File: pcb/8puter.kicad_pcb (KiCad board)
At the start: 2 copper layers, 13 parts

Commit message: Memory Module
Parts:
- removed C4: ~, Capacitor_THT:CP_Radial_D4.0mm_P1.50mm
- removed UMUX1: 74LS151, Package_DIP:DIP-18_W7.62mm_SMDSocket_SmallPads
- removed UPWR1 (x2): LT1761-1.5, Package_TO_SOT_SMD:TSOT-23-5
- added C1: C_Polarized_Small, Capacitor_THT:CP_Radial_D5.0mm_P2.00mm, F.Cu at (91.4, 106.7)
- added PWREG1: LT1761-1.5, Package_TO_SOT_SMD:TSOT-23-5, F.Cu at (94.0, 97.8)
- added PWREG2: LT1962-5, Package_SO:MSOP-8_3x3mm_P0.65mm, F.Cu at (94.0, 114.3)
- added UA1: ~, Package_SO:SO-14_3.9x8.65mm_P1.27mm, F.Cu at (135.9, 111.8)
- added UDEC1: 74HC237, Package_SO:SOP-16_4.4x10.4mm_P1.27mm, F.Cu at (144.8, 95.2)
- added UI1: ~, Package_SO:SO-16_3.9x9.9mm_P1.27mm, F.Cu at (144.8, 111.8)
- moved RAM3 72.5 mm to (175.3, 106.7), turned to 0 degrees
- moved C3 62.6 mm to (163.8, 58.4), turned to -90 degrees
- moved C3 57.5 mm to (154.9, 61.3), turned to -90 degrees
- moved RAM0 55.5 mm to (160.0, 106.7), turned to 0 degrees
- moved RAM1 53.9 mm to (160.0, 83.8), turned to 0 degrees
- moved RAM2 52.9 mm to (175.3, 83.8), turned to 0 degrees
- moved ROM1 47.4 mm to (102.9, 61.0)
- moved CPU1 23.9 mm to (132.1, 77.5), turned to 180 degrees
- moved UCLK1 3.18 mm to (105.4, 115.6)
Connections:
- net /D3 renamed DATA3
- net /D4 renamed DATA4
- net /D5 renamed DATA5
- net /D6 renamed DATA6
- net /D7 renamed DATA7
- C3 pad 1: unconnected-(C3-Pad1) -> /Power/BOARD_IN (x2)
- C3 pad 2: unconnected-(C3-Pad2) -> GND (x2)
- CPU1 pad 10: /A5 -> ADDR5
- CPU1 pad 11: /A6 -> ADDR6
- CPU1 pad 12: /A7 -> ADDR7
- CPU1 pad 13: /A8 -> ADDR8
- CPU1 pad 14: /A9 -> ADDR9
- CPU1 pad 15: /A10 -> ADDR10
- CPU1 pad 16: /A11 -> ADDR11
- CPU1 pad 19: /A12 -> ADDR12
- CPU1 pad 20: /A13 -> ADDR13
- CPU1 pad 21: /A14 -> ADDR14
- CPU1 pad 22: /A15 -> ADDR15
- CPU1 pad 28: /D2 -> DATA2
- CPU1 pad 29: /D1 -> DATA1
- CPU1 pad 30: /D0 -> DATA0
- CPU1 pad 34: unconnected-(CPU1-Pad34) -> A/~{D}
- CPU1 pad 4: /A0 -> ADDR0
- CPU1 pad 43: unconnected-(CPU1-Pad43) -> ~{IRQ}
- CPU1 pad 5: /A1 -> ADDR1
- CPU1 pad 7: /A2 -> ADDR2
- CPU1 pad 8: /A3 -> ADDR3
- CPU1 pad 9: /A4 -> ADDR4
- RAM0 pad 1: unconnected-(RAM0-Pad1) -> DATA1
- RAM0 pad 10: /Memory Unit/A2 -> ADDR2
- RAM0 pad 11: /Memory Unit/A1 -> ADDR1
- RAM0 pad 12: /Memory Unit/A0 -> ADDR0
- RAM0 pad 13: /Memory Unit/D0 -> DATA0
- RAM0 pad 14: /Memory Unit/D1 -> DATA1
- RAM0 pad 15: /Memory Unit/D2 -> DATA2
- RAM0 pad 17: /Memory Unit/D3 -> DATA0
- RAM0 pad 18: /Memory Unit/D4 -> DATA0
- RAM0 pad 19: /Memory Unit/D5 -> DATA0
- RAM0 pad 2: unconnected-(RAM0-Pad2) -> DATA0
- RAM0 pad 20: /Memory Unit/D6 -> DATA0
- RAM0 pad 21: /Memory Unit/D7 -> DATA0
- RAM0 pad 22: unconnected-(RAM0-Pad22) -> /Memory Unit/~{RAM0_EN}
- RAM0 pad 23: /Memory Unit/A10 -> ADDR10
- RAM0 pad 24: READ -> /Memory Unit/~{RAM0_EN}
- RAM0 pad 25: /Memory Unit/A11 -> ADDR11
- RAM0 pad 26: /Memory Unit/A9 -> ADDR9
- RAM0 pad 27: /Memory Unit/A8 -> ADDR8
- RAM0 pad 28: /Memory Unit/A13 -> ADDR13
- RAM0 pad 29: unconnected-(RAM0-Pad29) -> /Memory Unit/CPU_W/~{R}
- RAM0 pad 3: /Memory Unit/A14 -> ADDR14
- RAM0 pad 30: unconnected-(RAM0-Pad30) -> DATA2
- RAM0 pad 31: /Memory Unit/A15 -> ADDR15
- RAM0 pad 4: /Memory Unit/A12 -> ADDR12
- RAM0 pad 5: /Memory Unit/A7 -> ADDR7
- RAM0 pad 6: /Memory Unit/A6 -> ADDR6
- RAM0 pad 7: /Memory Unit/A5 -> ADDR5
- RAM0 pad 8: /Memory Unit/A4 -> ADDR4
- RAM0 pad 9: /Memory Unit/A3 -> ADDR3
- RAM1 pad 1: unconnected-(RAM1-Pad1) -> DATA1
- RAM1 pad 10: /Memory Unit/A2 -> ADDR2
- RAM1 pad 11: /Memory Unit/A1 -> ADDR1
- RAM1 pad 12: /Memory Unit/A0 -> ADDR0
- RAM1 pad 13: /Memory Unit/D0 -> DATA0
- RAM1 pad 14: /Memory Unit/D1 -> DATA1
- RAM1 pad 15: /Memory Unit/D2 -> DATA2
- RAM1 pad 17: /Memory Unit/D3 -> DATA0
- RAM1 pad 18: /Memory Unit/D4 -> DATA0
- RAM1 pad 19: /Memory Unit/D5 -> DATA0
- RAM1 pad 2: unconnected-(RAM1-Pad2) -> DATA0
- RAM1 pad 20: /Memory Unit/D6 -> DATA0
- RAM1 pad 21: /Memory Unit/D7 -> DATA0
- RAM1 pad 22: unconnected-(RAM1-Pad22) -> /Memory Unit/~{RAM1_EN}
- RAM1 pad 23: /Memory Unit/A10 -> ADDR10
- RAM1 pad 24: READ -> /Memory Unit/~{RAM1_EN}
- RAM1 pad 25: /Memory Unit/A11 -> ADDR11
- RAM1 pad 26: /Memory Unit/A9 -> ADDR9
- RAM1 pad 27: /Memory Unit/A8 -> ADDR8
- RAM1 pad 28: /Memory Unit/A13 -> ADDR13
- RAM1 pad 29: unconnected-(RAM1-Pad29) -> /Memory Unit/CPU_W/~{R}
- RAM1 pad 3: /Memory Unit/A14 -> ADDR14
- RAM1 pad 30: unconnected-(RAM1-Pad30) -> DATA2
- RAM1 pad 31: /Memory Unit/A15 -> ADDR15
- RAM1 pad 4: /Memory Unit/A12 -> ADDR12
- RAM1 pad 5: /Memory Unit/A7 -> ADDR7
- RAM1 pad 6: /Memory Unit/A6 -> ADDR6
- RAM1 pad 7: /Memory Unit/A5 -> ADDR5
- RAM1 pad 8: /Memory Unit/A4 -> ADDR4
- RAM1 pad 9: /Memory Unit/A3 -> ADDR3
- RAM2 pad 1: unconnected-(RAM2-Pad1) -> DATA1
- RAM2 pad 10: /Memory Unit/A2 -> ADDR2
- RAM2 pad 11: /Memory Unit/A1 -> ADDR1
- RAM2 pad 12: /Memory Unit/A0 -> ADDR0
- RAM2 pad 13: /Memory Unit/D0 -> DATA0
- RAM2 pad 14: /Memory Unit/D1 -> DATA1
- RAM2 pad 15: /Memory Unit/D2 -> DATA2
- RAM2 pad 17: /Memory Unit/D3 -> DATA0
- RAM2 pad 18: /Memory Unit/D4 -> DATA0
- RAM2 pad 19: /Memory Unit/D5 -> DATA0
- RAM2 pad 2: unconnected-(RAM2-Pad2) -> DATA0
- RAM2 pad 20: /Memory Unit/D6 -> DATA0
- RAM2 pad 21: /Memory Unit/D7 -> DATA0
- RAM2 pad 22: unconnected-(RAM2-Pad22) -> /Memory Unit/~{RAM2_EN}
- RAM2 pad 23: /Memory Unit/A10 -> ADDR10
- RAM2 pad 24: READ -> /Memory Unit/~{RAM2_EN}
- RAM2 pad 25: /Memory Unit/A11 -> ADDR11
- RAM2 pad 26: /Memory Unit/A9 -> ADDR9
- RAM2 pad 27: /Memory Unit/A8 -> ADDR8
- RAM2 pad 28: /Memory Unit/A13 -> ADDR13
- RAM2 pad 29: unconnected-(RAM2-Pad29) -> /Memory Unit/CPU_W/~{R}
- RAM2 pad 3: /Memory Unit/A14 -> ADDR14
- RAM2 pad 30: unconnected-(RAM2-Pad30) -> DATA2
- RAM2 pad 31: /Memory Unit/A15 -> ADDR15
- RAM2 pad 4: /Memory Unit/A12 -> ADDR12
- RAM2 pad 5: /Memory Unit/A7 -> ADDR7
- RAM2 pad 6: /Memory Unit/A6 -> ADDR6
- RAM2 pad 7: /Memory Unit/A5 -> ADDR5
- RAM2 pad 8: /Memory Unit/A4 -> ADDR4
- RAM2 pad 9: /Memory Unit/A3 -> ADDR3
- RAM3 pad 1: unconnected-(RAM3-Pad1) -> DATA1
- RAM3 pad 10: /Memory Unit/A2 -> ADDR2
- RAM3 pad 11: /Memory Unit/A1 -> ADDR1
- RAM3 pad 12: /Memory Unit/A0 -> ADDR0
- RAM3 pad 13: /Memory Unit/D0 -> DATA0
- RAM3 pad 14: /Memory Unit/D1 -> DATA1
- RAM3 pad 15: /Memory Unit/D2 -> DATA2
- RAM3 pad 17: /Memory Unit/D3 -> DATA0
- RAM3 pad 18: /Memory Unit/D4 -> DATA0
- RAM3 pad 19: /Memory Unit/D5 -> DATA0
- RAM3 pad 2: unconnected-(RAM3-Pad2) -> DATA0
- RAM3 pad 20: /Memory Unit/D6 -> DATA0
- RAM3 pad 21: /Memory Unit/D7 -> DATA0
- RAM3 pad 22: unconnected-(RAM3-Pad22) -> /Memory Unit/~{RAM3_EN}
- RAM3 pad 23: /Memory Unit/A10 -> ADDR10
- RAM3 pad 24: READ -> /Memory Unit/~{RAM3_EN}
- RAM3 pad 25: /Memory Unit/A11 -> ADDR11
- RAM3 pad 26: /Memory Unit/A9 -> ADDR9
- RAM3 pad 27: /Memory Unit/A8 -> ADDR8
- RAM3 pad 28: /Memory Unit/A13 -> ADDR13
- RAM3 pad 29: unconnected-(RAM3-Pad29) -> /Memory Unit/CPU_W/~{R}
- RAM3 pad 3: /Memory Unit/A14 -> ADDR14
- RAM3 pad 30: unconnected-(RAM3-Pad30) -> DATA2
- RAM3 pad 31: /Memory Unit/A15 -> ADDR15
- RAM3 pad 4: /Memory Unit/A12 -> ADDR12
- RAM3 pad 5: /Memory Unit/A7 -> ADDR7
- RAM3 pad 6: /Memory Unit/A6 -> ADDR6
- RAM3 pad 7: /Memory Unit/A5 -> ADDR5
- RAM3 pad 8: /Memory Unit/A4 -> ADDR4
- RAM3 pad 9: /Memory Unit/A3 -> ADDR3
- ROM1 pad 10: /Memory Unit/A2 -> ADDR2
- ROM1 pad 11: /Memory Unit/A1 -> ADDR1
- ROM1 pad 12: /Memory Unit/A0 -> ADDR0
- ROM1 pad 13: /Memory Unit/D0 -> DATA0
- ROM1 pad 14: /Memory Unit/D1 -> DATA1
- ROM1 pad 15: /Memory Unit/D2 -> DATA2
- ROM1 pad 17: /Memory Unit/D3 -> DATA0
- ROM1 pad 18: /Memory Unit/D4 -> DATA0
- ROM1 pad 19: /Memory Unit/D5 -> DATA0
- ROM1 pad 2: unconnected-(ROM1-Pad2) -> /Memory Unit/CROM_EN
- ROM1 pad 20: /Memory Unit/D6 -> DATA0
- ROM1 pad 21: /Memory Unit/D7 -> DATA0
- ROM1 pad 22: unconnected-(ROM1-Pad22) -> /Memory Unit/ROM_EN
- ROM1 pad 23: /Memory Unit/A10 -> ADDR10
- ROM1 pad 24: READ -> R/~{W}
- ROM1 pad 25: /Memory Unit/A11 -> ADDR11
- ROM1 pad 26: /Memory Unit/A9 -> ADDR9
- ROM1 pad 27: /Memory Unit/A8 -> ADDR8
- ROM1 pad 28: /Memory Unit/A13 -> ADDR13
- ROM1 pad 29: /Memory Unit/A14 -> ADDR14
- ROM1 pad 3: /Memory Unit/A15 -> ADDR15
- ROM1 pad 31: READ -> unconnected-(ROM1-Pad31)
- ROM1 pad 4: /Memory Unit/A12 -> ADDR12
- ROM1 pad 5: /Memory Unit/A7 -> ADDR7
- ROM1 pad 6: /Memory Unit/A6 -> ADDR6
- ROM1 pad 7: /Memory Unit/A5 -> ADDR5
- ROM1 pad 8: /Memory Unit/A4 -> ADDR4
- ROM1 pad 9: /Memory Unit/A3 -> ADDR3
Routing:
- net ADDR4: track 0.00 -> 21.7 mm, vias 0 -> 2
- net ADDR5: track 0.00 -> 21.7 mm, vias 0 -> 2
- net ADDR6: track 0.00 -> 21.5 mm, vias 0 -> 2
- net unconnected-(CPU1-Pad41): track 19.5 -> 0.00 mm
- net unconnected-(CPU1-Pad42): track 18.7 -> 0.00 mm
- net unconnected-(UPWR1-Pad4): track 16.7 -> 0.00 mm
- net unconnected-(CPU1-Pad43): track 16.3 -> 0.00 mm
- net unconnected-(CPU1-Pad44): track 15.5 -> 0.00 mm
- net RESET: track 14.8 -> 0.00 mm
- net unconnected-(UPWR1-Pad5): track 12.7 -> 0.00 mm
- net /A10: track 12.2 -> 0.00 mm
- net /A14: track 8.19 -> 0.00 mm
- net unconnected-(URAM3-Pad30): track 0.50 -> 0.00 mm
- net (no net): vias 17 -> 0

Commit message: Bus control
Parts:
- removed PWREG1: LT1761-1.5, Package_TO_SOT_SMD:TSOT-23-5
- removed UCLK1: ACO-10MHz-A, Oscillator:Oscillator_DIP-14_LargePads
- added BDT1: 74AC245, Package_SO:TSSOP-20_4.4x6.5mm_P0.65mm, F.Cu at (140.0, 124.4)
- added CRYSTAL0: ACO-10MHz-A, Oscillator:Oscillator_DIP-14_LargePads, F.Cu at (105.2, 118.1)
- added J1: PWR-DC, Connector_BarrelJack:BarrelJack_CUI_PJ-063AH_Horizontal, F.Cu at (175.8, 45.1)
- added LATCH1: 74AC573, Package_SO:TSSOP-20_4.4x6.5mm_P0.65mm, F.Cu at (95.5, 125.5)
- added RP1: 1K, Resistor_THT:R_Array_SIP9, F.Cu at (102.6, 135.6)
- added RP2: 1K, Resistor_THT:R_Array_SIP9, F.Cu at (92.5, 53.4)
- added RP3: 1K, Resistor_THT:R_Array_SIP9, F.Cu at (110.7, 103.6)
- added RP4: 1K, Resistor_THT:R_Array_SIP9, F.Cu at (102.6, 140.0)
- added RP5: 1K, Resistor_THT:R_Array_SIP9, F.Cu at (97.0, 49.3)
- added U1: 74AC00, Package_SO:TSSOP-14_4.4x5mm_P0.65mm, F.Cu at (129.6, 139.5)
- added U3: DS1135Z, Package_SO:SO-8_5.3x6.2mm_P1.27mm, F.Cu at (130.4, 124.3)
- added U6: MAX811MEUS-T, Package_TO_SOT_SMD:SOT-143, F.Cu at (151.3, 122.6)
- C1: value C_Polarized_Small -> 1uF
- CPU1: footprint Package_QFP:PQFP-44_10x10mm_P0.8mm -> Package_DIP:DIP-40_W25.4mm_Socket_LongPads
- moved PWREG2 97.0 mm to (173.2, 58.4)
- moved ROM1 23.7 mm to (79.3, 59.7)
- moved CPU1 14.0 mm to (132.1, 91.4)
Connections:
- C1 pad 1: /Power/BOARD_IN -> /Power/PWR
- CPU1 pad 1: unconnected-(CPU1-Pad1) -> ~{NMI}
- CPU1 pad 23: DATA7 -> /DBA7
- CPU1 pad 24: DATA6 -> /DBA6
- CPU1 pad 25: DATA5 -> /DBA5
- CPU1 pad 26: DATA4 -> /DBA4
- CPU1 pad 27: DATA3 -> /DBA3
- CPU1 pad 28: DATA2 -> /DBA2
- CPU1 pad 29: DATA1 -> /DBA1
- CPU1 pad 3: VDD -> +5V
- CPU1 pad 30: DATA0 -> /DBA0
- CPU1 pad 31: VDD -> +5V
- CPU1 pad 34: A/~{D} -> BE
- PWREG2 pad 8: /Power/BOARD_IN -> /Power/PWR
- RAM0 pad 1: DATA1 -> ADDR0
- RAM0 pad 17: DATA0 -> DATA3
- RAM0 pad 18: DATA0 -> DATA4
- RAM0 pad 19: DATA0 -> DATA5
- RAM0 pad 2: DATA0 -> ADDR0
- RAM0 pad 20: DATA0 -> DATA6
- RAM0 pad 21: DATA0 -> DATA7
- RAM0 pad 30: DATA2 -> ADDR0
- RAM1 pad 1: DATA1 -> ADDR0
- RAM1 pad 17: DATA0 -> DATA3
- RAM1 pad 18: DATA0 -> DATA4
- RAM1 pad 19: DATA0 -> DATA5
- RAM1 pad 2: DATA0 -> ADDR0
- RAM1 pad 20: DATA0 -> DATA6
- RAM1 pad 21: DATA0 -> DATA7
- RAM1 pad 30: DATA2 -> ADDR0
- RAM2 pad 1: DATA1 -> ADDR0
- RAM2 pad 17: DATA0 -> DATA3
- RAM2 pad 18: DATA0 -> DATA4
- RAM2 pad 19: DATA0 -> DATA5
- RAM2 pad 2: DATA0 -> ADDR0
- RAM2 pad 20: DATA0 -> DATA6
- RAM2 pad 21: DATA0 -> DATA7
- RAM2 pad 30: DATA2 -> ADDR0
- RAM3 pad 1: DATA1 -> ADDR0
- RAM3 pad 17: DATA0 -> DATA3
- RAM3 pad 18: DATA0 -> DATA4
- RAM3 pad 19: DATA0 -> DATA5
- RAM3 pad 2: DATA0 -> ADDR0
- RAM3 pad 20: DATA0 -> DATA6
- RAM3 pad 21: DATA0 -> DATA7
- RAM3 pad 30: DATA2 -> ADDR0
- ROM1 pad 17: DATA0 -> DATA3
- ROM1 pad 18: DATA0 -> DATA4
- ROM1 pad 19: DATA0 -> DATA5
- ROM1 pad 20: DATA0 -> DATA6
- ROM1 pad 21: DATA0 -> DATA7
- UA1 pad 4: A/~{D} -> /Memory Unit/Address Decoder/CPU_A/~{D}
- UDEC1 pad 1: DATA0 -> ADDR0
- UDEC1 pad 2: DATA1 -> ADDR1
- UDEC1 pad 3: DATA2 -> ADDR2
- UDEC1 pad 6: A/~{D} -> /Memory Unit/Address Decoder/CPU_A/~{D}
- UI1 pad 13: A/~{D} -> /Memory Unit/Address Decoder/CPU_A/~{D}
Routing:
- net ADDR4: track 21.7 -> 0.00 mm, vias 2 -> 0
- net ADDR5: track 21.7 -> 0.00 mm, vias 2 -> 0
- net ADDR6: track 21.5 -> 0.00 mm, vias 2 -> 0

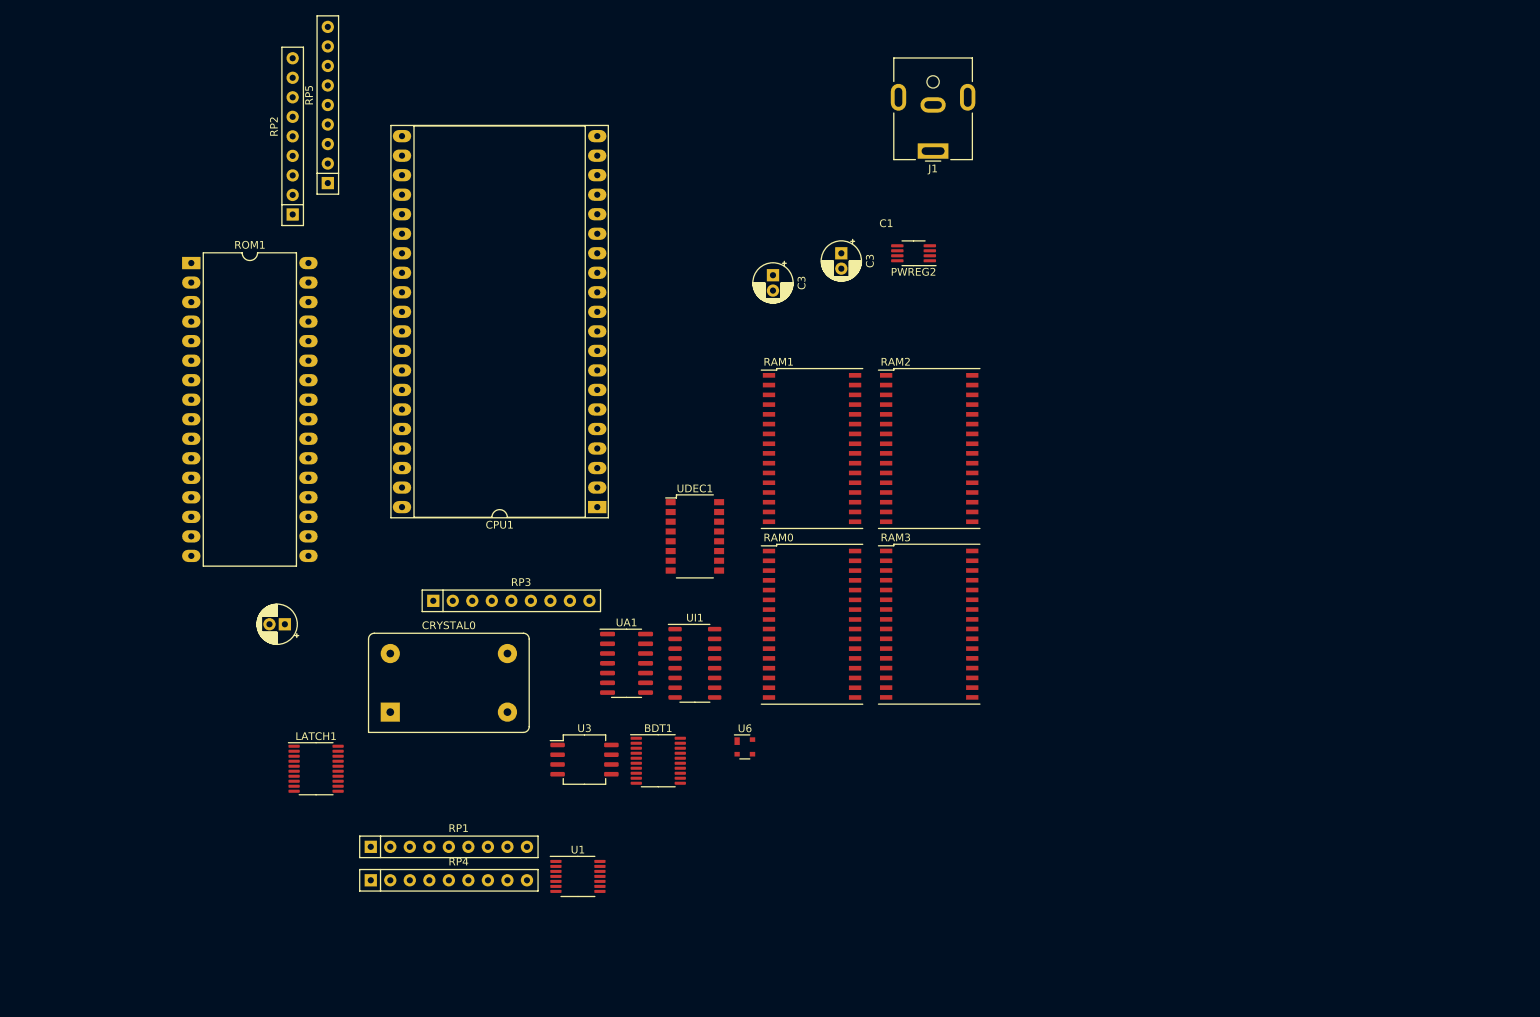
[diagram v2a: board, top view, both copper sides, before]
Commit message: New address decoder
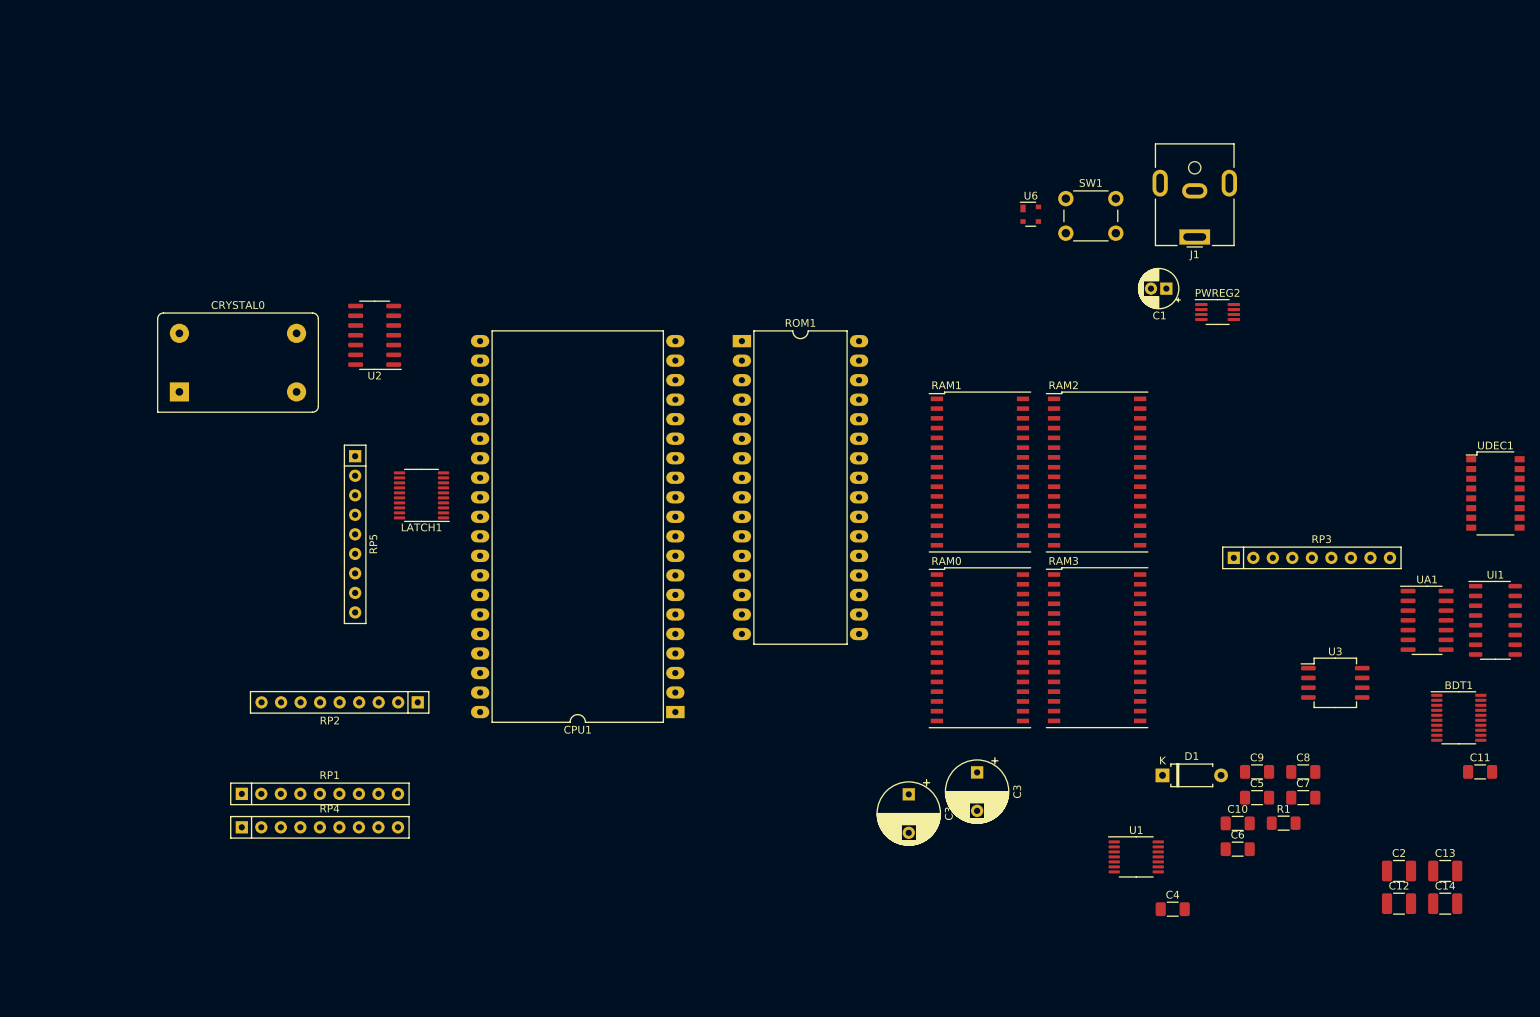
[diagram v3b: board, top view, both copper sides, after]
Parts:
- added C10: 100nF, Capacitor_SMD:C_1206_3216Metric_Pad1.33x1.80mm_HandSolder, F.Cu at (215.4, 132.6)
- added C11: 10nF, Capacitor_SMD:C_1206_3216Metric_Pad1.33x1.80mm_HandSolder, F.Cu at (246.9, 125.9)
- added C12: 1uF, Capacitor_SMD:C_1210_3225Metric_Pad1.33x2.70mm_HandSolder, F.Cu at (236.4, 143.0)
- added C13: 1uF, Capacitor_SMD:C_1210_3225Metric_Pad1.33x2.70mm_HandSolder, F.Cu at (242.4, 138.8)
- added C14: 1uF, Capacitor_SMD:C_1210_3225Metric_Pad1.33x2.70mm_HandSolder, F.Cu at (242.4, 143.0)
- added C2: 1uF, Capacitor_SMD:C_1210_3225Metric_Pad1.33x2.70mm_HandSolder, F.Cu at (236.4, 138.8)
- added C4: 10uF, Capacitor_SMD:C_1206_3216Metric_Pad1.33x1.80mm_HandSolder, F.Cu at (206.9, 143.7)
- added C5: 10nF, Capacitor_SMD:C_1206_3216Metric_Pad1.33x1.80mm_HandSolder, F.Cu at (217.9, 129.2)
- added C6: 10nF, Capacitor_SMD:C_1206_3216Metric_Pad1.33x1.80mm_HandSolder, F.Cu at (215.4, 135.9)
- added C7: 10nF, Capacitor_SMD:C_1206_3216Metric_Pad1.33x1.80mm_HandSolder, F.Cu at (223.9, 129.2)
- added C8: 10nF, Capacitor_SMD:C_1206_3216Metric_Pad1.33x1.80mm_HandSolder, F.Cu at (223.9, 125.9)
- added C9: 100nF, Capacitor_SMD:C_1206_3216Metric_Pad1.33x1.80mm_HandSolder, F.Cu at (217.9, 125.9)
- added D1: 1N5817, Diode_THT:D_A-405_P7.62mm_Horizontal, F.Cu at (205.6, 126.3)
- added R1: ~, Resistor_SMD:R_1206_3216Metric_Pad1.30x1.75mm_HandSolder, F.Cu at (221.4, 132.6)
- added SW1: RESET_SW, Button_Switch_THT:SW_PUSH_6mm_H13mm, F.Cu at (193.0, 51.3)
- added U2: 74HC74, Package_SO:SOIC-14_3.9x8.7mm_P1.27mm, F.Cu at (103.1, 69.1)
- C3 (x2): value C_Polarized_Small -> 10uF; footprint Capacitor_THT:CP_Radial_D5.0mm_P2.00mm -> Capacitor_THT:CP_Radial_D8.0mm_P5.00mm
- CPU1: value W65C816SxQ -> W65C816SxP; footprint Package_DIP:DIP-40_W25.4mm_Socket_LongPads -> Package_DIP:DIP-40_W25.4mm_LongPads
- moved C1 122.7 mm to (206.1, 63.0)
- moved BDT1 104.3 mm to (244.2, 118.8)
- moved UA1 104.3 mm to (240.0, 106.2)
- moved RP3 104.3 mm to (214.9, 98.0)
- moved UDEC1 104.3 mm to (248.9, 89.7)
- moved UI1 104.3 mm to (248.9, 106.2)
- moved U3 98.2 mm to (228.1, 114.3)
- moved U6 78.6 mm to (188.5, 53.3)
- moved U1 72.7 mm to (202.2, 136.9)
- moved ROM1 72.3 mm to (150.9, 69.8)
- moved C3 69.8 mm to (172.6, 128.8)
- moved C3 69.8 mm to (181.5, 126.0)
- moved RP2 65.5 mm to (108.7, 116.8), turned to 180 degrees
- moved CRYSTAL0 49.9 mm to (77.7, 76.5)
- moved PWREG2 40.3 mm to (212.8, 66.1), turned to 0 degrees
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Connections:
- C3 pad 1: /Power/BOARD_IN -> /Power/PWR (x2)
- CPU1 pad 1: ~{NMI} -> unconnected-(CPU1-Pad1)
- CPU1 pad 10: ADDR5 -> ADDR1
- CPU1 pad 11: ADDR6 -> ADDR2
- CPU1 pad 12: ADDR7 -> ADDR3
- CPU1 pad 13: ADDR8 -> ADDR4
- CPU1 pad 14: ADDR9 -> ADDR5
- CPU1 pad 15: ADDR10 -> ADDR6
- CPU1 pad 16: ADDR11 -> ADDR7
- CPU1 pad 17: GND -> ADDR8
- CPU1 pad 18: GND -> ADDR9
- CPU1 pad 19: ADDR12 -> ADDR10
- CPU1 pad 2: unconnected-(CPU1-Pad2) -> RDY
- CPU1 pad 20: ADDR13 -> ADDR11
- CPU1 pad 21: ADDR14 -> GND
- CPU1 pad 22: ADDR15 -> ADDR12
- CPU1 pad 23: /DBA7 -> ADDR13
- CPU1 pad 24: /DBA6 -> ADDR14
- CPU1 pad 25: /DBA5 -> ADDR15
- CPU1 pad 26: /DBA4 -> /DBA7
- CPU1 pad 27: /DBA3 -> /DBA6
- CPU1 pad 28: /DBA2 -> /DBA5
- CPU1 pad 29: /DBA1 -> /DBA4
- CPU1 pad 3: +5V -> ~{ABORT}
- CPU1 pad 30: /DBA0 -> /DBA3
- CPU1 pad 31: +5V -> /DBA2
- CPU1 pad 32: R/~{W} -> /DBA1
- CPU1 pad 33: unconnected-(CPU1-Pad33) -> /DBA0
- CPU1 pad 34: BE -> R/~{W}
- CPU1 pad 35: CLOCK -> EMU
- CPU1 pad 36: unconnected-(CPU1-Pad36) -> BE
- CPU1 pad 37: unconnected-(CPU1-Pad37) -> CLOCK
- CPU1 pad 38: RESET -> unconnected-(CPU1-Pad38)
- CPU1 pad 39: GND -> unconnected-(CPU1-Pad39)
- CPU1 pad 4: ADDR0 -> ~{IRQ}
- CPU1 pad 40: unconnected-(CPU1-Pad40) -> RESET
- CPU1 pad 5: ADDR1 -> unconnected-(CPU1-Pad5)
- CPU1 pad 6: unconnected-(CPU1-Pad6) -> ~{NMI}
- CPU1 pad 7: ADDR2 -> unconnected-(CPU1-Pad7)
- CPU1 pad 8: ADDR3 -> +5V
- CPU1 pad 9: ADDR4 -> ADDR0
- CRYSTAL0 pad 8: Net-(CRYSTAL0-Pad8) -> /Clock/CRYSTAL
- RAM0 pad 32: VCC -> +5V
- RAM1 pad 32: VCC -> +5V
- RAM2 pad 32: VCC -> +5V
- RAM3 pad 32: VCC -> +5V
